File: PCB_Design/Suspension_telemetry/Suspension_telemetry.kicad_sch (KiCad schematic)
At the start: 23 parts, among them J11 530480310, J12 530480410, J2 Conn_01x03_Pin, J3 112J-TDAR-R01, J4 Conn_02x04_Top_Bottom, J6 Conn_01x08_Socket, J7 530480510, J8 530480310, J9 530480410, U5 USBLC6-2SC6

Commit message: pcv v2 finished
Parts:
- removed J11, J8: 530480310, molex_conn:530480310, symbol 530480310:530480310
- removed J12, J9: 530480410, molex_conn:530480410, symbol 530480410:530480410
- removed J2: Conn_01x03_Pin, Connector_PinHeader_1.27mm:PinHeader_1x03_P1.27mm_Vertical, symbol Connector:Conn_01x03_Pin
- removed J4: Conn_02x04_Top_Bottom, Connector_PinSocket_2.54mm:PinSocket_2x04_P2.54mm_Vertical, symbol connector_my_2x4:Conn_02x04_Top_Bottom_v2
- removed J6: Conn_01x08_Socket, Connector_PinSocket_2.54mm:PinSocket_1x08_P2.54mm_Vertical, symbol Connector:Conn_01x08_Socket
- removed J7: 530480510, molex_conn:530480510, symbol 530480510:530480510
- removed R9 (x2): 6,8k, Resistor_SMD:R_0603_1608Metric_Pad0.98x0.95mm_HandSolder, symbol Device:R_Small
- removed R9 (x2): 4,7k, Resistor_SMD:R_0603_1608Metric_Pad0.98x0.95mm_HandSolder, symbol Device:R_Small
- added C14 (x4): 100n, Capacitor_SMD:C_0603_1608Metric_Pad1.08x0.95mm_HandSolder, symbol Device:C_Small
- added J2: 125SH-A-04-TS, molex_conn:125SHA04TS, symbol MOLEX_4:125SH-A-04-TS
- added J4: 530481010, 530481010, symbol MOLEX_10_pin:530481010
- added J5: 280384-1, BUTTON_CONN:2803841, symbol BUTTON_CONN:280384-1
- added J7: Conn_02x03_Top_Bottom, Connector_PinHeader_2.54mm:PinHeader_2x03_P2.54mm_Vertical, symbol Connector_Generic:Conn_02x03_Top_Bottom
- added N1, N2, N3: Housing, Symbol:CE-Logo_8.5x6mm_SilkScreen, symbol Mechanical:Housing
- added R9 (x2): 6,8k, Resistor_SMD:R_0603_1608Metric_Pad0.98x0.95mm_HandSolder, symbol Device:R_Small
- added R9 (x2): 1k, Resistor_SMD:R_0603_1608Metric_Pad0.98x0.95mm_HandSolder, symbol Device:R_Small
- added R9 (x3): 4,7k, Resistor_SMD:R_0603_1608Metric_Pad0.98x0.95mm_HandSolder, symbol Device:R_Small
- added R9 (x2): 100k, Resistor_SMD:R_0603_1608Metric_Pad0.98x0.95mm_HandSolder, symbol Device:R_Small
- added R9: 10k, Resistor_SMD:R_0603_1608Metric_Pad0.98x0.95mm_HandSolder, symbol Device:R_Small
- added U4: ADXL343, Package_LGA:LGA-14_3x5mm_P0.8mm_LayoutBorder1x6y, symbol Sensor_Motion:ADXL343
- added U6: AT24CS254-SSHM, Package_SO:SOIC-8_3.9x4.9mm_P1.27mm, symbol Memory_EEPROM:AT24CS64-SSHM
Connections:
- net +3.3V: now also J2.4, J5.2, J7.2 (Pin_2), R9.1, U4.1 (Vdd_I/O), U4.6 (Vs), U6.8 (VCC)
- net +3.3VA: now also J4.4
- net +5VA: now also J4.9
- net 5V_USB: now also R9.1
- net GND: now also C14.2, C14.2, C14.2, C14.2, J2.3, J4.10, J4.3, J5.1, J5.8, J7.3 (Pin_3), R9.1, R9.1, R9.2, R9.2, U4.2 (GND), U4.4 (GND), U4.5 (GND), U6.1 (A0), U6.2 (A1), U6.3 (A2), U6.4 (GND), U6.7 (WP)
- net I2C1_SCL: now also J2.2, U4.14 (SCL/SCLK), U6.6 (SCL)
- net I2C1_SDA: now also J2.1, U4.13 (SDA/SDI/SDIO), U6.5 (SDA)
- net Power_Stabilizer_3_3V/V_in_P: now also R9.2
- net PRESSURE_REAR_OUT: now reaches R9.1
- net PRESSURE_REAR_OUT: now also J4.2
- net ADC2_IN14 renamed PRESSURE_SENSOR_REAR
- new net: R9.2, U4.7 (~{CS})
- new net: R9.2, U4.12 (SDO/ADDR)
- new net ACCELEROMETER_INT0: U4.8 (INT1)
- new net BATTERY_LEVEL: R9.1, R9.2
- new net BRAKE_SENSOR_LEFT: J4.7
- new net BRAKE_SENSOR_RIGHT: J4.8
- new net CHARGE_DETECTION: R9.1, R9.2
- new net LB_PRE_DEB: J5.3, R9.2
- new net LEFT_BUTTON: C14.1, R9.1
- new net NRST: C14.1, J5.7, J7.1 (Pin_1)
- new net PRESSURE_FRONT_OUT: J4.1, R9.1
- new net PRESSURE_SENSOR_FRONT: R9.1, R9.2
- new net PWR_SWITCH_IN: J5.4
- new net PWR_SWITCH_OUT: C14.1, J5.6
- new net RB_PRE_DEB: J5.5, R9.2
- new net RIGHT_BUTTON: C14.1, R9.1
- new net SWDCLK: J7.6 (Pin_6)
- new net SWDIO: J7.5 (Pin_5)
- new net SWO: J7.4 (Pin_4)
- new net TRAVEL_SENOR_REAR: J4.5
- new net TRAVEL_SENSOR_FRONT: J4.6
- no-connect marks 8 -> 3
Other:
- sheet Power_Stabilizer_3_3V ports: added none; removed V_Out_M, V_in_M
- sheet Power_Stabilizer_5V ports: added none; removed V_Out_M, V_in_M
- sheet Power_Supply ports: added PWR_SWITCH_IN, PWR_SWITCH_OUT; removed 5V_USB_IN_M, V_BAT_2S_M
- sheet STM32F446RET6_Base ports: added ACCELEROMETER_INT0, BATTERY_LEVEL, BRAKE_SENSOR_LEFT, BRAKE_SENSOR_RIGHT, CHARGE_DETECTION, LEFT_BUTTON, NRST, PRESSURE_SENSOR_FRONT, PRESSURE_SENSOR_REAR, RIGHT_BUTTON, SWDCLK, SWDIO, SWO, TRAVEL_SENOR_REAR, TRAVEL_SENSOR_FRONT; removed ADC2_IN1, ADC2_IN13, ADC2_IN14, ADC2_IN4, ADC3_IN0, PA5, PB0, USART_RX, USART_TX
- sheet USB_C ports: added none; removed V_5V_GND_C
- note removed: "ESP8266-01S"
- note removed: "TRAVEL SENSOR"
- moved on the sheet: R9

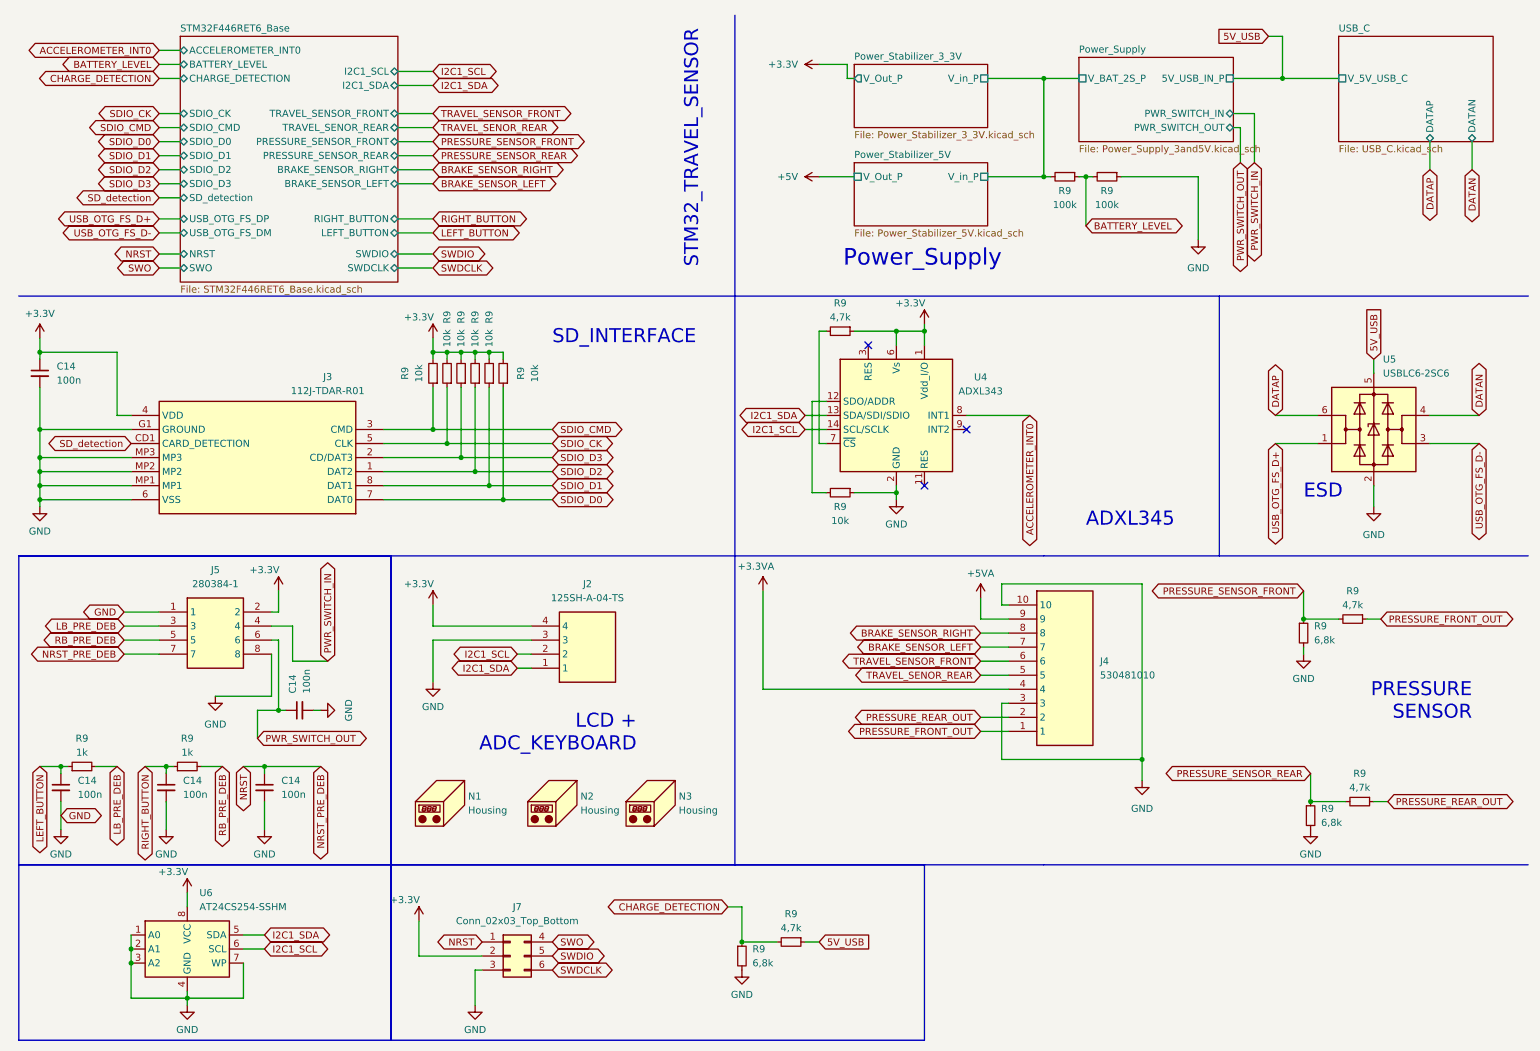
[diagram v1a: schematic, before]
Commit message: adding swnsor mounts
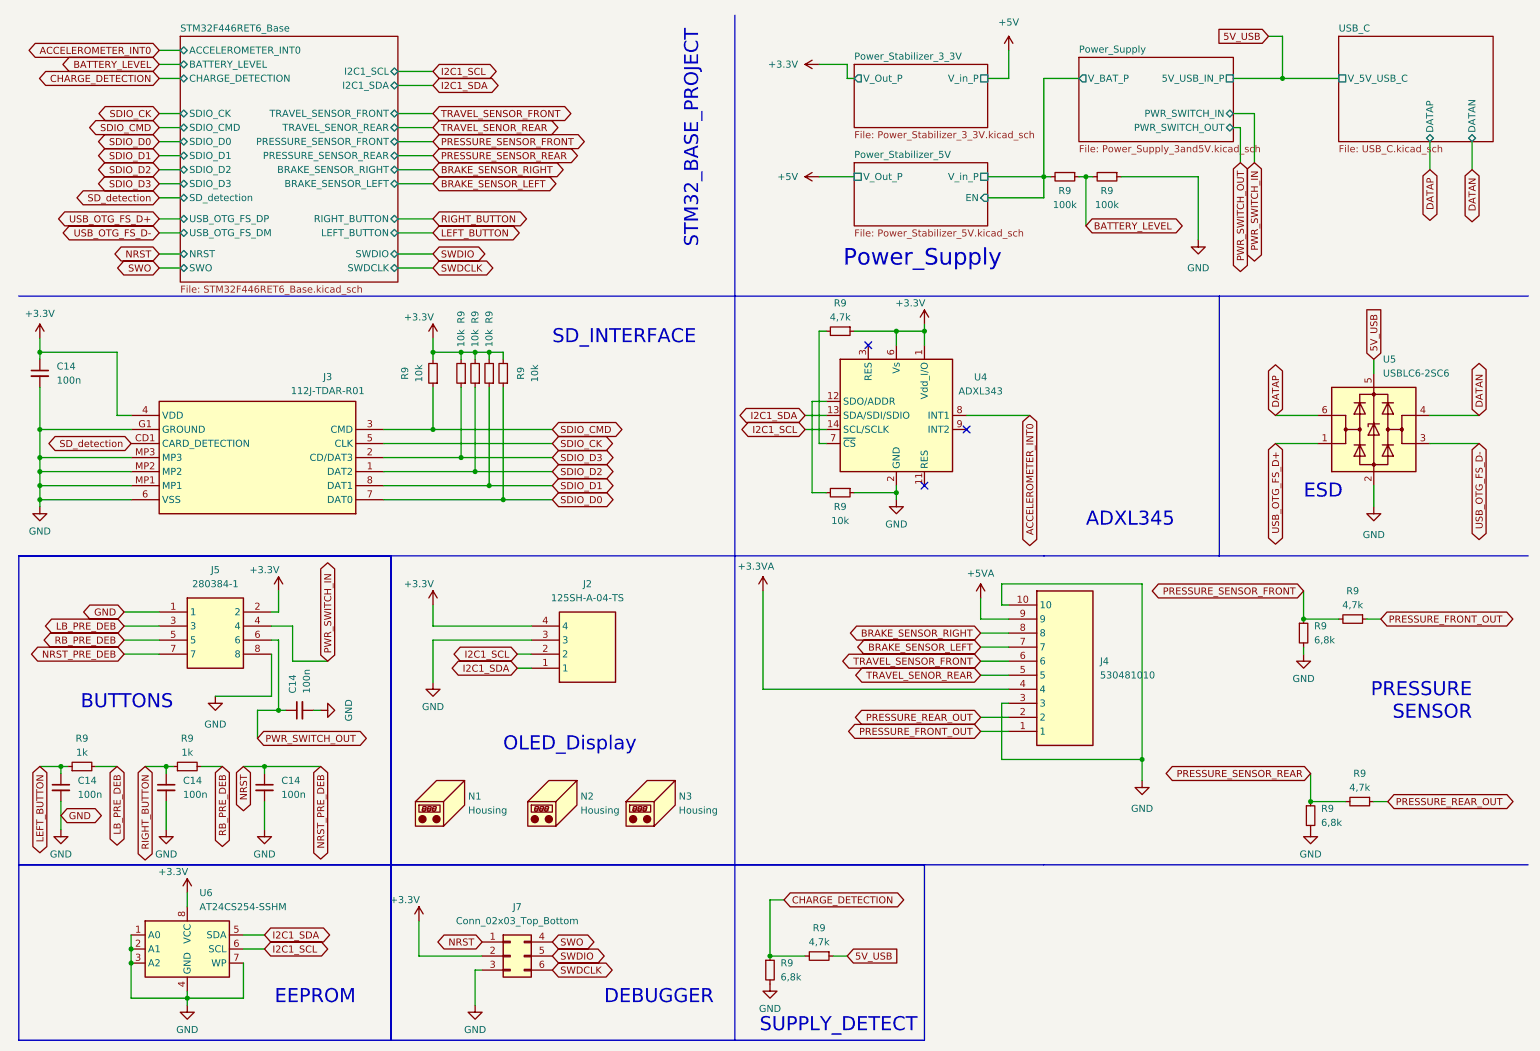
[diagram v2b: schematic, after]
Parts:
- removed R9: 10k, Resistor_SMD:R_0603_1608Metric_Pad0.98x0.95mm_HandSolder, symbol Device:R_Small
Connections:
- net Power_Stabilizer_3_3V/V_in_P renamed Power_Stabilizer_5V/EN
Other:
- sheet Power_Stabilizer_5V ports: added EN; removed none
- sheet Power_Supply ports: added V_BAT_P; removed V_BAT_2S_P
- note added: "BUTTONS"
- note added: "DEBUGGER"
- note added: "EEPROM"
- note added: "OLED_Display"
- note added: "STM32_BASE_PROJECT"
- note added: "SUPPLY_DETECT"
- note removed: "LCD + ADC_KEYBOARD"
- note removed: "STM32_TRAVEL_SENSOR"
- moved on the sheet: R9
